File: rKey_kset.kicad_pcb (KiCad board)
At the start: 2 copper layers, 48.3 x 51.3 mm, 25 parts, among them J1 Conn_01x08, Q1 BC337, Q2 BC337, Q3 BC337, Q4 BC337, Q5 BC337, Q6 BC337

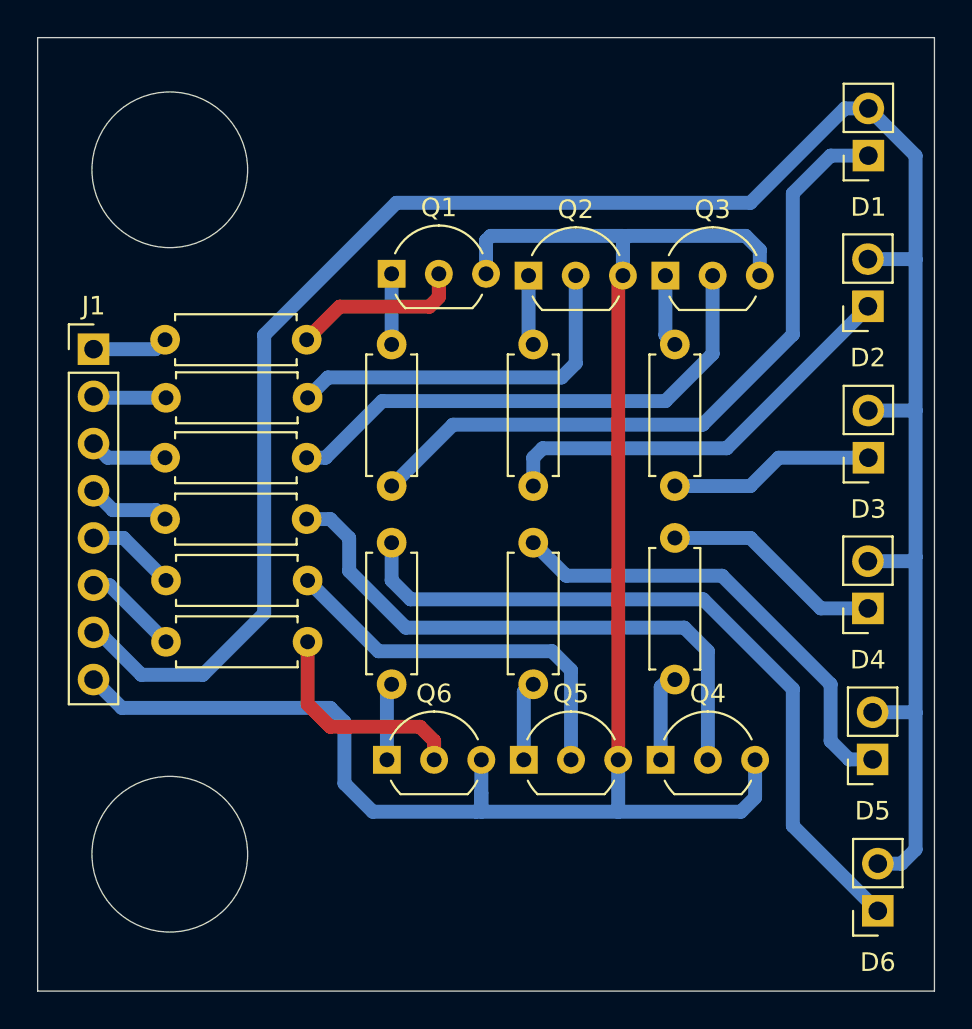
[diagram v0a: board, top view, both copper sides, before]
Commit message: Wrong holes size and reducing whole circuit size
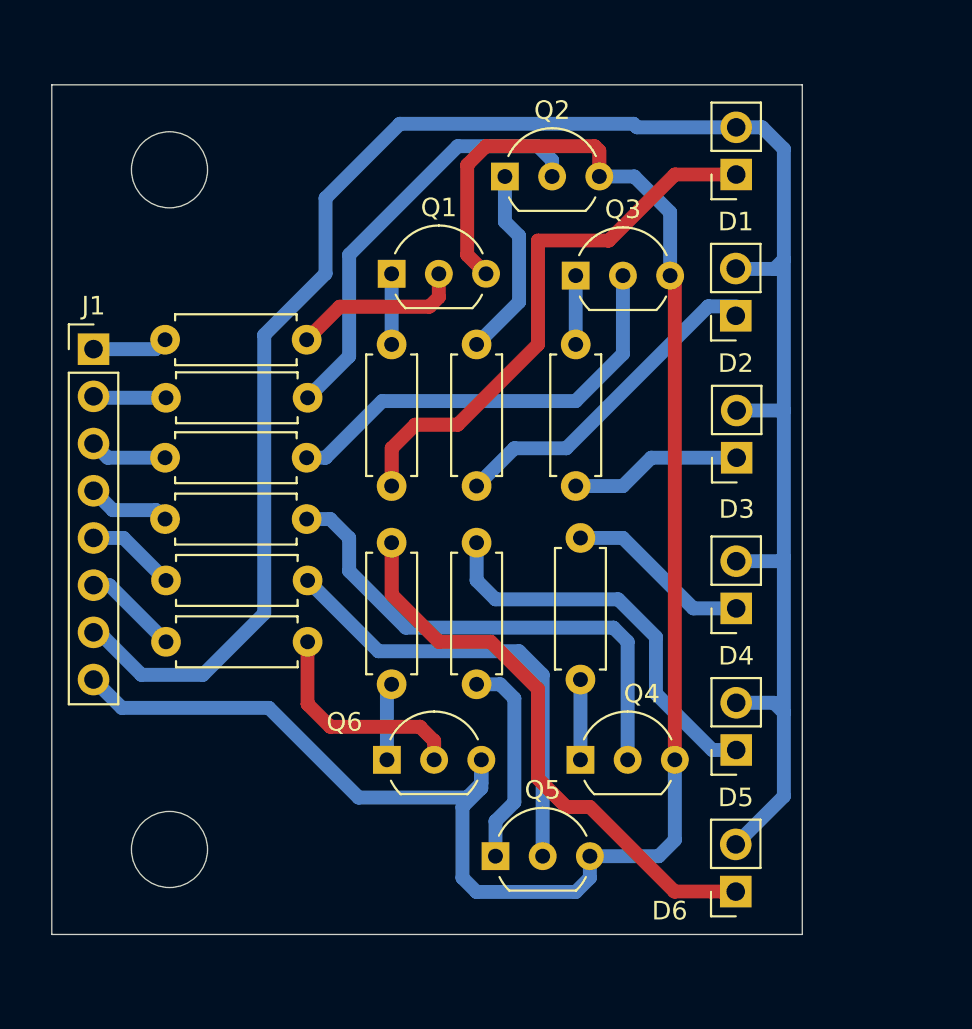
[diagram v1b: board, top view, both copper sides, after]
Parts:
- moved D6 7.71 mm to (146.5, 109.2)
- moved D5 7.36 mm to (146.6, 101.6)
- moved D1 7.18 mm to (146.6, 70.6)
- moved D2 7.13 mm to (146.5, 78.2)
- moved D4 7.09 mm to (146.6, 94.0)
- moved D3 7.09 mm to (146.6, 85.9)
- moved Q2 5.48 mm to (134.1, 70.7)
- moved Q5 5.41 mm to (133.6, 107.3)
- moved R6 5.33 mm to (137.9, 79.8)
- moved R9 5.08 mm to (138.2, 97.8)
- moved Q3 4.83 mm to (137.9, 76.1)
- moved Q4 4.32 mm to (138.2, 102.1)
- moved R11 3.05 mm to (132.6, 98.0)
- moved R5 3.05 mm to (132.6, 79.8)
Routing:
- net Net-(D6-Pad1): track 39.9 -> 30.8 mm
- net Net-(D1-Pad1): track 37.5 -> 29.9 mm
- net Net-(Q5-Pad1): track 4.38 -> 11.3 mm
- net Net-(Q2-Pad1): track 3.81 -> 10.3 mm
- net Net-(D1-Pad2): track 117.4 -> 111.4 mm
- net Net-(D2-Pad1): track 22.9 -> 18.0 mm
- net Net-(Q3-Pad2): track 28.4 -> 23.5 mm
- net Net-(Q4-Pad2): track 31.4 -> 27.4 mm
- net Net-(Q5-Pad2): track 21.0 -> 24.5 mm
- net Net-(D5-Pad1): track 24.9 -> 21.6 mm
- net Net-(Q2-Pad2): track 19.9 -> 23.1 mm
- net Net-(D4-Pad1): track 12.0 -> 9.95 mm
- net Net-(D3-Pad1): track 11.0 -> 9.29 mm
- net GND: track 97.9 -> 99.2 mm
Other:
- board size 48.3 x 51.3 mm -> 40.4 x 45.7 mm

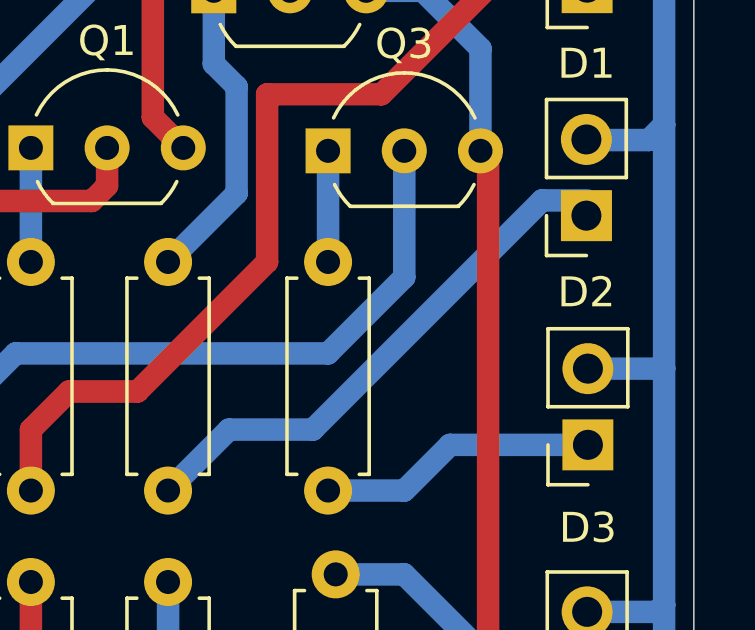
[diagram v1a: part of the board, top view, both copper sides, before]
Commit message: change: resistors values tuned to reduce the required current
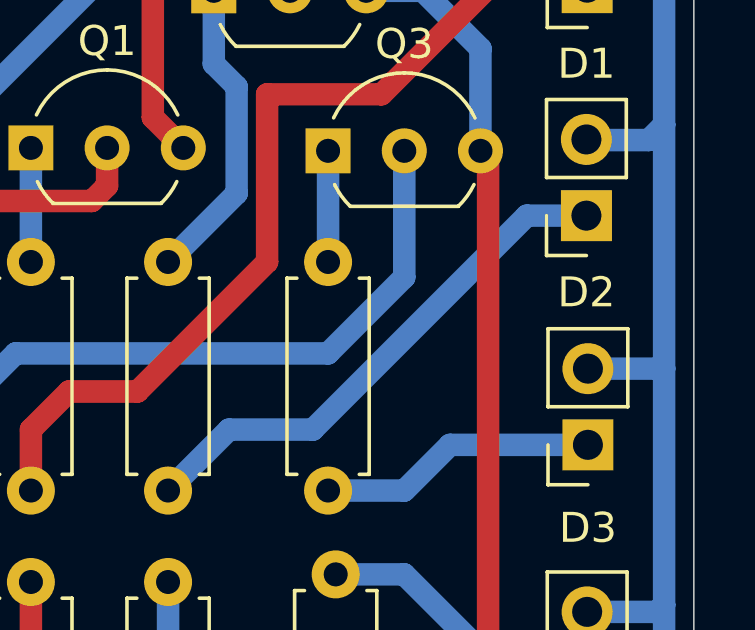
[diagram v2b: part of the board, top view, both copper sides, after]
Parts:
- R1, R10, R2, R4, R7, R8: value 5K -> 10K
- R11, R12, R3, R5, R6, R9: value 500 -> 3K

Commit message: Layout enhancement
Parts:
- moved Q5 12.3 mm to (122.3, 102.4), turned to -90 degrees
- moved Q4 9.40 mm to (128.8, 102.4), turned to -90 degrees
- moved Q6 4.72 mm to (125.0, 98.3), turned to 180 degrees
- moved Q3 4.06 mm to (133.9, 76.1)
- moved D6 3.38 mm to (143.7, 107.4)
- moved D5 3.25 mm to (143.7, 100.1)
- moved D4 3.11 mm to (143.7, 92.7)
- moved D3 2.89 mm to (143.7, 85.3)
- moved D2 2.83 mm to (143.7, 78.0)
- moved D1 2.82 mm to (143.7, 70.6)
- moved Q1 2.29 mm to (125.7, 75.9)
- moved J1 1.83 mm to (112.0, 78.2)
- moved R2 1.83 mm to (115.9, 80.8)
- moved R4 1.83 mm to (115.8, 84.0)
- moved R7 1.83 mm to (115.8, 87.3)
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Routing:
- net GND: track 99.2 -> 89.9 mm
- net Net-(Q6-Pad2): track 12.0 -> 4.81 mm
- net Net-(Q4-Pad1): track 4.32 -> 10.0 mm
- net Net-(Q4-Pad2): track 27.4 -> 22.2 mm
- net Net-(Q1-Pad2): track 9.32 -> 6.14 mm
- net Net-(D1-Pad2): track 111.4 -> 108.3 mm
- net Net-(D5-Pad1): track 21.6 -> 19.0 mm
- net Net-(Q5-Pad2): track 24.5 -> 22.0 mm
- net Net-(D1-Pad1): track 29.9 -> 27.7 mm
- net Net-(D4-Pad1): track 9.95 -> 7.85 mm
- net Net-(D3-Pad1): track 9.29 -> 7.68 mm
- net Net-(Q3-Pad1): track 3.70 -> 5.26 mm
- net Net-(Q6-Pad1): track 4.38 -> 3.15 mm
- net Net-(Q1-Pad1): track 3.80 -> 4.76 mm
- net Net-(D2-Pad1): track 17.7 -> 16.8 mm
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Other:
- board size 40.4 x 45.7 mm -> 37.3 x 43.9 mm
